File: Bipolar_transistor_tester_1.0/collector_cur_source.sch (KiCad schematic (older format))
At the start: 38 parts

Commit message: tester up
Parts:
- removed Q?: AO3400A, Package_TO_SOT_SMD:SOT-23, symbol Transistor_FET:AO3400A
- removed Q?: AO3401A, Package_TO_SOT_SMD:SOT-23, symbol Transistor_FET:AO3401A
- added C1, C2, C3, C4: 100n, Capacitor_SMD:C_0805_2012Metric, symbol Device:C
- added Q3: IRFR9024 [DPAK], Package_TO_SOT_SMD:TO-252-2, symbol Transistor_FET:IRF4905
- added Q4: IRF640 [DPAK], Package_TO_SOT_SMD:TO-252-2, symbol Transistor_FET:IRF540N
- added R13, R14, R19, R2, R20, R23, R24, R25, R26: 1k 1%, Resistor_SMD:R_0805_2012Metric, symbol Device:R
- added U11, U12: CPC1977, OptoDevice:i4-PAC, symbol Relay_SolidState:CPC1977
- added U4: PVN012, Package_DIP:DIP-6_W7.62mm, symbol Relay_SolidState:PVN012
- D5, D6: renamed from D?; value 1N4740A -> 1N4744A
- R10, R9: renamed from R?; value 50k -> 51k
- R15, R16: renamed from R?; value 270 -> 2.2k
- R21, R22: renamed from R?; value 20k 1% -> 10k 1%
- gave numbers to parts that had none: 26
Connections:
- net +15V: now also C2.1
- net +24V: now also C3.1
- net -15V: now also C1.1
- net -24V: now also C4.1
- net GND: now also C1.2, C2.2, C3.2, C4.2
- net out: now also U11.1, U12.1
- net at D6.2 (A), IC2.2, R12.2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: now also Q4.3 (S)
- net at IC1.2, R11.2, R17.2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: now also D5.1 (K), Q3.3 (S); no longer D5.2 (A)
- net at U5.1: now also R13.2
- net 1_ccs2: now reaches U5.2
- net 1_ccs2: now also U6.2
- net at U7.1: now also R19.2
- net 1_ccs3: now reaches U7.2
- net 1_ccs3: now also U8.2
- net at U9.1: now also R23.2
- net 1_ccs4: now reaches U9.2
- net 1_ccs4: now also U10.2
- net at U6.1: now also R14.2
- net at U10.1: now also R24.2
- net at D6.1 (K), R16.1: now also Q4.1 (G)
- net at R15.1: now also D5.2 (A), Q3.1 (G); no longer D5.1 (K)
- net dac_in: no longer names the net of R1.1, U3.3 (+), U3.5 (+)
- net dac_in: now also U4.6
- new net: Q3.2 (D), Q4.2 (D), U11.2, U12.2
- new net: R26.2, U12.4
- new net: R25.2, U11.4
- new net: R2.2, U4.1
- new net 1_ccs1: U4.2
- new net 1_ccs5: U11.3, U12.3
- new net 1_com_an: R13.1, R14.1, R19.1, R2.1, R20.1, R23.1, R24.1, R25.1, R26.1
- new net dac0: U4.4
- no-connect marks 6 -> 11
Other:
- moved on the sheet: D1, D2, D3, D4, D5, D6, IC1, IC2, Q1, Q2, R1, R10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

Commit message: tester up
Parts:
- removed R12: 2 1%, Resistor_SMD:R_0805_2012Metric, symbol Device:R
- added R14: 2 1% 0.5W, Resistor_THT:R_Axial_DIN0309_L9.0mm_D3.2mm_P12.70mm_Horizontal, symbol Device:R
- Q3: value IRFR9024 [DPAK] -> IRFR9024
- Q4: value IRF640 [DPAK] -> IRF640
- R13: renamed from R11; value 2 1% -> 2 1% 0.5W; footprint Resistor_SMD:R_0805_2012Metric -> Resistor_THT:R_Axial_DIN0309_L9.0mm_D3.2mm_P12.70mm_Horizontal
- renumbered R8 to R10, R9 to R11, R10 to R12, R13 to R15, R14 to R16, R15 to R17, R16 to R18, R17 to R19, R18 to R20, R19 to R21, R20 to R22, R21 to R23, R22 to R24, R23 to R25, R24 to R26, R25 to R27, R26 to R28, R1 to R3, R2 to R4, R3 to R5, R4 to R6, R5 to R7, R6 to R8, R7 to R9
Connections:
- net +15V: no longer R7.1
- net +24V: now also R7.1
- net -15V: no longer R10.2
- net -24V: now also R10.2
- net at D6.2 (A), IC2.2, Q4.3 (S)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: now also R14.1
- net at R22.2: now also U8.1
- net at U6.6: now also R14.2
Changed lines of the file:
@@
 Sheet 2 11
 Title ""
-Date ""
+Date "2022-04-25"
 Rev ""
 Comp ""
@@
 	1100 4350 1100 4150
 $Comp
-L Device:R R6
+L Device:R R8
 U 1 1 626AADC7
 P 3700 2950
-F 0 "R6" H 3770 2996 50  0000 L CNN
+F 0 "R8" H 3770 2996 50  0000 L CNN
 F 1 "1k 1%" H 3770 2905 50  0000 L CNN
 F 2 "Resistor_SMD:R_0805_2012Metric" V 3630 2950 50  0001 C CNN
@@
 $EndComp
 $Comp
-L Device:R R5
+L Device:R R7
 U 1 1 626AF1BA
 P 3700 1950
-F 0 "R5" H 3770 1996 50  0000 L CNN
+F 0 "R7" H 3770 1996 50  0000 L CNN
 F 1 "1k 1%" H 3770 1905 50  0000 L CNN
 F 2 "Resistor_SMD:R_0805_2012Metric" V 3630 1950 50  0001 C CNN
@@
 $EndComp
 $Comp
-L Device:R R3
+L Device:R R5
 U 1 1 626B6D1A
 P 2800 2450
-F 0 "R3" V 2593 2450 50  0000 C CNN
+F 0 "R5" V 2593 2450 50  0000 C CNN
 F 1 "270" V 2684 2450 50  0000 C CNN
 F 2 "Resistor_SMD:R_0805_2012Metric" V 2730 2450 50  0001 C CNN
@@
 	3700 2750 3700 2650
 $Comp
-L Device:R R4
+L Device:R R6
 U 1 1 626C4ED7
 P 2850 5050
-F 0 "R4" V 2643 5050 50  0000 C CNN
+F 0 "R6" V 2643 5050 50  0000 C CNN
 F 1 "270" V 2734 5050 50  0000 C CNN
 F 2 "Resistor_SMD:R_0805_2012Metric" V 2780 5050 50  0001 C CNN
@@
 	2550 5050 2700 5050
 $Comp
-L Device:R R7
+L Device:R R9
 U 1 1 626C8015
 P 3850 4550
-F 0 "R7" H 3920 4596 50  0000 L CNN
+F 0 "R9" H 3920 4596 50  0000 L CNN
 F 1 "1k 1%" H 3920 4505 50  0000 L CNN
 F 2 "Resistor_SMD:R_0805_2012Metric" V 3780 4550 50  0001 C CNN
@@
 	1    0    0    -1
 $EndComp
-$Comp
-L power:+15V #PWR011
-U 1 1 626C90AB
-P 3700 1600
-F 0 "#PWR011" H 3700 1450 50  0001 C CNN
-F 1 "+15V" H 3715 1773 50  0000 C CNN
-F 2 "" H 3700 1600 50  0001 C CNN
-F 3 "" H 3700 1600 50  0001 C CNN
-	1    3700 1600
-	1    0    0    -1
-$EndComp
 Wire Wire Line
 	3700 1600 3700 1800
 $Comp
-L Device:R R8
+L Device:R R10
 U 1 1 626CB4E6
 P 3850 5550
-F 0 "R8" H 3920 5596 50  0000 L CNN
+F 0 "R10" H 3920 5596 50  0000 L CNN
 F 1 "1k 1%" H 3920 5505 50  0000 L CNN
 F 2 "Resistor_SMD:R_0805_2012Metric" V 3780 5550 50  0001 C CNN
@@
 Wire Wire Line
 	3850 4150 3850 4400
-$Comp
-L power:-15V #PWR013
-U 1 1 626CEEF2
-P 3850 6000
-F 0 "#PWR013" H 3850 6100 50  0001 C CNN
-F 1 "-15V" H 3865 6173 50  0000 C CNN
-F 2 "" H 3850 6000 50  0001 C CNN
-F 3 "" H 3850 6000 50  0001 C CNN
-	1    3850 6000
-	-1   0    0    1
-$EndComp
 Wire Wire Line
 	3850 5700 3850 6000
@@
 	1750 2350 1950 2350
 $Comp
-L Device:R R1
+L Device:R R3
 U 1 1 626D8FC2
 P 1400 2550
-F 0 "R1" H 1470 2596 50  0000 L CNN
+F 0 "R3" H 1470 2596 50  0000 L CNN
 F 1 "100k" H 1470 2505 50  0000 L CNN
 F 2 "Resistor_SMD:R_0805_2012Metric" V 1330 2550 50  0001 C CNN
@@
 P 5250 4350
 AR Path="/625CBC7B/626F7564" Ref="R?"  Part="1"
-AR Path="/62558810/626F7564" Ref="R10"  Part="1"
-F 0 "R10" H 5320 4396 50  0000 L CNN
+AR Path="/62558810/626F7564" Ref="R12"  Part="1"
+F 0 "R12" H 5320 4396 50  0000 L CNN
 F 1 "51k" H 5320 4305 50  0000 L CNN
 F 2 "Resistor_SMD:R_0805_2012Metric" V 5180 4350 50  0001 C CNN
@@
 P 5250 1750
 AR Path="/625CBC7B/62717692" Ref="R?"  Part="1"
-AR Path="/62558810/62717692" Ref="R9"  Part="1"
-F 0 "R9" H 5320 1796 50  0000 L CNN
+AR Path="/62558810/62717692" Ref="R11"  Part="1"
+F 0 "R11" H 5320 1796 50  0000 L CNN
 F 1 "51k" H 5320 1705 50  0000 L CNN
 F 2 "Resistor_SMD:R_0805_2012Metric" V 5180 1750 50  0001 C CNN
@@
 $EndComp
 $Comp
-L Device:R R11
+L Device:R R13
 U 1 1 62727C59
 P 6200 2250
-F 0 "R11" H 6270 2296 50  0000 L CNN
-F 1 "2 1%" H 6270 2205 50  0000 L CNN
-F 2 "Resistor_SMD:R_0805_2012Metric" V 6130 2250 50  0001 C CNN
+F 0 "R13" H 6270 2296 50  0000 L CNN
+F 1 "2 1% 0.5W" H 6270 2205 50  0000 L CNN
+F 2 "Resistor_THT:R_Axial_DIN0309_L9.0mm_D3.2mm_P12.70mm_Horizontal" V 6130 2250 50  0001 C CNN
 F 3 "~" H 6200 2250 50  0001 C CNN
 	1    6200 2250
@@
 $EndComp
 $Comp
-L Device:R R17
+L Device:R R19
 U 1 1 6273D379
 P 7650 2250
-F 0 "R17" H 7720 2296 50  0000 L CNN
+F 0 "R19" H 7720 2296 50  0000 L CNN
 F 1 "200 1%" H 7720 2205 50  0000 L CNN
 F 2 "Resistor_SMD:R_0805_2012Metric" V 7580 2250 50  0001 C CNN
@@
 $EndComp
 $Comp
-L Device:R R21
+L Device:R R23
 U 1 1 6273D8AB
 P 9050 2250
-F 0 "R21" H 9120 2296 50  0000 L CNN
+F 0 "R23" H 9120 2296 50  0000 L CNN
 F 1 "10k 1%" H 9120 2205 50  0000 L CNN
 F 2 "Resistor_SMD:R_0805_2012Metric" V 8980 2250 50  0001 C CNN
@@
 $EndComp
 $Comp
-L Device:R R12
-U 1 1 627A3DF1
-P 6300 5350
-F 0 "R12" H 6370 5396 50  0000 L CNN
-F 1 "2 1%" H 6370 5305 50  0000 L CNN
-F 2 "Resistor_SMD:R_0805_2012Metric" V 6230 5350 50  0001 C CNN
-F 3 "~" H 6300 5350 50  0001 C CNN
-	1    6300 5350
-	1    0    0    1
-$EndComp
-$Comp
-L Device:R R18
+L Device:R R20
 U 1 1 627A3DF7
 P 7650 5350
-F 0 "R18" H 7720 5396 50  0000 L CNN
+F 0 "R20" H 7720 5396 50  0000 L CNN
 F 1 "200 1%" H 7720 5305 50  0000 L CNN
 F 2 "Resistor_SMD:R_0805_2012Metric" V 7580 5350 50  0001 C CNN
@@
 $EndComp
 $Comp
-L Device:R R22
+L Device:R R24
 U 1 1 627A3DFD
 P 9050 5350
-F 0 "R22" H 9120 5396 50  0000 L CNN
+F 0 "R24" H 9120 5396 50  0000 L CNN
 F 1 "10k 1%" H 9120 5305 50  0000 L CNN
 F 2 "Resistor_SMD:R_0805_2012Metric" V 8980 5350 50  0001 C CNN
@@
 	6050 2700 6200 2700
 $Comp
-L Device:R R16
+L Device:R R18
 U 1 1 627E417A
 P 7000 4100
-F 0 "R16" V 6793 4100 50  0000 C CNN
+F 0 "R18" V 6793 4100 50  0000 C CNN
 F 1 "2.2k" V 6884 4100 50  0000 C CNN
 F 2 "Resistor_SMD:R_0805_2012Metric" V 6930 4100 50  0001 C CNN
@@
 $EndComp
 $Comp
-L Device:R R15
+L Device:R R17
 U 1 1 627E52A8
 P 7000 3500
-F 0 "R15" V 6793 3500 50  0000 C CNN
+F 0 "R17" V 6793 3500 50  0000 C CNN
 F 1 "2.2k" V 6884 3500 50  0000 C CNN
 F 2 "Resistor_SMD:R_0805_2012Metric" V 6930 3500 50  0001 C CNN
@@
 P 7750 4100
 F 0 "Q4" H 7955 4146 50  0000 L CNN
-F 1 "IRF640 [DPAK]" H 7955 4055 50  0000 L CNN
+F 1 "IRF640" H 7955 4055 50  0000 L CNN
 F 2 "Package_TO_SOT_SMD:TO-252-2" H 8000 4025 50  0001 L CIN
 F 3 "" H 7750 4100 50  0001 L CNN
@@
 P 7750 3500
 F 0 "Q3" H 7955 3546 50  0000 L CNN
-F 1 "IRFR9024 [DPAK]" H 7955 3455 50  0000 L CNN
+F 1 "IRFR9024" H 7955 3455 50  0000 L CNN
 F 2 "Package_TO_SOT_SMD:TO-252-2" H 7950 3425 50  0001 L CIN
 F 3 "" H 7750 3500 50  0001 L CNN
@@
 $EndComp
 $Comp
-L Device:R R2
+L Device:R R4
 U 1 1 627516BC
 P 1750 1100
-F 0 "R2" H 1820 1146 50  0000 L CNN
+F 0 "R4" H 1820 1146 50  0000 L CNN
 F 1 "1k 1%" H 1820 1055 50  0000 L CNN
 F 2 "Resistor_SMD:R_0805_2012Metric" V 1680 1100 50  0001 C CNN
@@
 	1950 950  1750 950
 $Comp
-L Device:R R19
+L Device:R R21
 U 1 1 6275DF20
 P 8300 2750
-F 0 "R19" H 8370 2796 50  0000 L CNN
+F 0 "R21" H 8370 2796 50  0000 L CNN
 F 1 "1k 1%" H 8370 2705 50  0000 L CNN
 F 2 "Resistor_SMD:R_0805_2012Metric" V 8230 2750 50  0001 C CNN
@@
 	8300 2600 8300 2550
 $Comp
-L Device:R R13
+L Device:R R15
 U 1 1 6276D4C8
 P 6900 2750
-F 0 "R13" H 6970 2796 50  0000 L CNN
+F 0 "R15" H 6970 2796 50  0000 L CNN
 F 1 "1k 1%" H 6970 2705 50  0000 L CNN
 F 2 "Resistor_SMD:R_0805_2012Metric" V 6830 2750 50  0001 C CNN
@@
 	6900 2600 6900 2550
 $Comp
-L Device:R R23
+L Device:R R25
 U 1 1 6277CC66
 P 9650 2750
-F 0 "R23" H 9720 2796 50  0000 L CNN
+F 0 "R25" H 9720 2796 50  0000 L CNN
 F 1 "1k 1%" H 9720 2705 50  0000 L CNN
 F 2 "Resistor_SMD:R_0805_2012Metric" V 9580 2750 50  0001 C CNN
@@
 	9650 2600 9650 2550
 $Comp
-L Device:R R14
+L Device:R R16
 U 1 1 62788745
 P 6900 4850
-F 0 "R14" H 6970 4896 50  0000 L CNN
+F 0 "R16" H 6970 4896 50  0000 L CNN
 F 1 "1k 1%" H 6970 4805 50  0000 L CNN
 F 2 "Resistor_SMD:R_0805_2012Metric" V 6830 4850 50  0001 C CNN
@@
 	6900 5050 6900 5000
 $Comp
-L Device:R R20
+L Device:R R22
 U 1 1 62799EB5
 P 8300 4850
-F 0 "R20" H 8370 4896 50  0000 L CNN
+F 0 "R22" H 8370 4896 50  0000 L CNN
 F 1 "1k 1%" H 8370 4805 50  0000 L CNN
 F 2 "Resistor_SMD:R_0805_2012Metric" V 8230 4850 50  0001 C CNN
@@
 	8250 4700 8300 4700
 $Comp
-L Device:R R24
+L Device:R R26
 U 1 1 6279F93D
 P 9650 4850
-F 0 "R24" H 9720 4896 50  0000 L CNN
+F 0 "R26" H 9720 4896 50  0000 L CNN
 F 1 "1k 1%" H 9720 4805 50  0000 L CNN
 F 2 "Resistor_SMD:R_0805_2012Metric" V 9580 4850 50  0001 C CNN
@@
 	9650 5000 9650 5050
 $Comp
-L Device:R R26
+L Device:R R28
 U 1 1 627AB630
 P 10200 4600
-F 0 "R26" H 10270 4646 50  0000 L CNN
+F 0 "R28" H 10270 4646 50  0000 L CNN
 F 1 "1k 1%" H 10270 4555 50  0000 L CNN
 F 2 "Resistor_SMD:R_0805_2012Metric" V 10130 4600 50  0001 C CNN
@@
 	10200 4450 10200 4400
 $Comp
-L Device:R R25
+L Device:R R27
 U 1 1 627B8223
 P 10200 2950
-F 0 "R25" H 10270 2996 50  0000 L CNN
+F 0 "R27" H 10270 2996 50  0000 L CNN
 F 1 "1k 1%" H 10270 2905 50  0000 L CNN
 F 2 "Resistor_SMD:R_0805_2012Metric" V 10130 2950 50  0001 C CNN
@@
 NoConn ~ 5150 2950
 NoConn ~ 5150 2150
+$Comp
+L power:+24V #PWR011
+U 1 1 62689B44
+P 3700 1600
+F 0 "#PWR011" H 3700 1450 50  0001 C CNN
+F 1 "+24V" H 3715 1773 50  0000 C CNN
+F 2 "" H 3700 1600 50  0001 C CNN
+F 3 "" H 3700 1600 50  0001 C CNN
+	1    3700 1600
+	1    0    0    -1
+$EndComp
+$Comp
+L power:-24V #PWR013
+U 1 1 6268A10F
+P 3850 6000
+F 0 "#PWR013" H 3850 6100 50  0001 C CNN
+F 1 "-24V" H 3865 6173 50  0000 C CNN
+F 2 "" H 3850 6000 50  0001 C CNN
+F 3 "" H 3850 6000 50  0001 C CNN
+	1    3850 6000
+	-1   0    0    1
+$EndComp
+$Comp
+L Device:R R14
+U 1 1 6269D7EE
+P 6300 5350
+F 0 "R14" H 6370 5396 50  0000 L CNN
+F 1 "2 1% 0.5W" H 6370 5305 50  0000 L CNN
+F 2 "Resistor_THT:R_Axial_DIN0309_L9.0mm_D3.2mm_P12.70mm_Horizontal" V 6230 5350 50  0001 C CNN
+F 3 "~" H 6300 5350 50  0001 C CNN
+	1    6300 5350
+	1    0    0    -1
+$EndComp
+Wire Wire Line
+	8300 5050 8300 5000
 $EndSCHEMATC

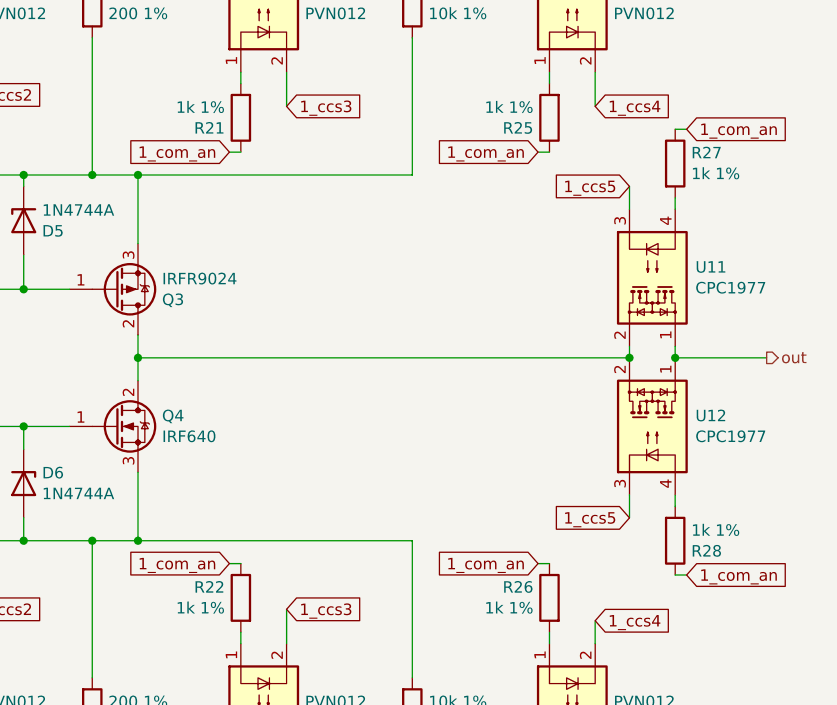
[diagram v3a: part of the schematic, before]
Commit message: edit resistors cpc1977
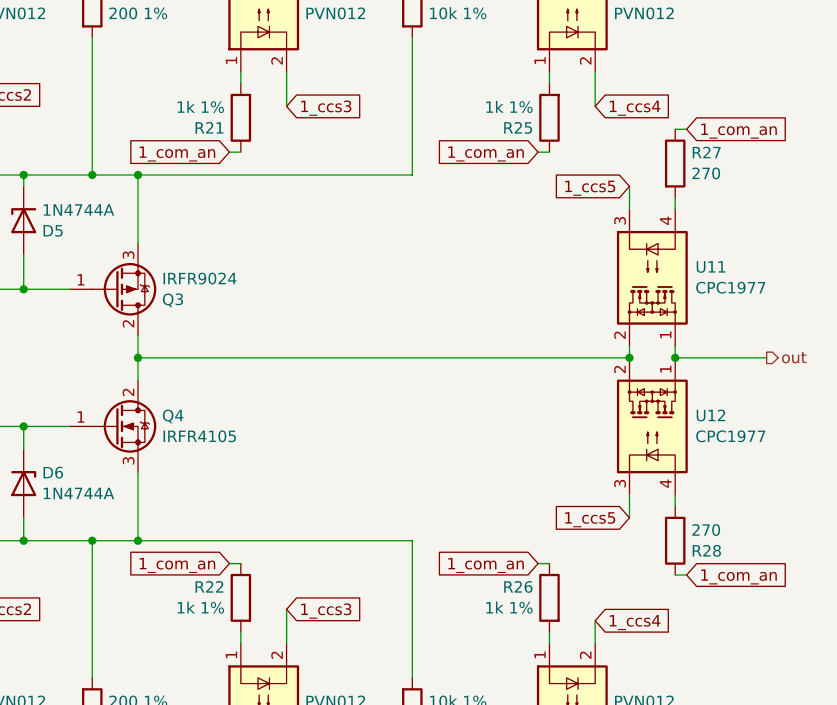
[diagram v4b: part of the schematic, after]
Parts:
- Q4: value IRF640 -> IRFR4105
- R27, R28: value 1k 1% -> 270
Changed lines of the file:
@@
 P 7750 4100
 F 0 "Q4" H 7955 4146 50  0000 L CNN
-F 1 "IRF640" H 7955 4055 50  0000 L CNN
+F 1 "IRFR4105" H 7955 4055 50  0000 L CNN
 F 2 "Package_TO_SOT_SMD:TO-252-2" H 8000 4025 50  0001 L CIN
 F 3 "" H 7750 4100 50  0001 L CNN
@@
 P 10200 4600
 F 0 "R28" H 10270 4646 50  0000 L CNN
-F 1 "1k 1%" H 10270 4555 50  0000 L CNN
+F 1 "270" H 10270 4555 50  0000 L CNN
 F 2 "Resistor_SMD:R_0805_2012Metric" V 10130 4600 50  0001 C CNN
 F 3 "~" H 10200 4600 50  0001 C CNN
@@
 P 10200 2950
 F 0 "R27" H 10270 2996 50  0000 L CNN
-F 1 "1k 1%" H 10270 2905 50  0000 L CNN
+F 1 "270" H 10270 2905 50  0000 L CNN
 F 2 "Resistor_SMD:R_0805_2012Metric" V 10130 2950 50  0001 C CNN
 F 3 "~" H 10200 2950 50  0001 C CNN
